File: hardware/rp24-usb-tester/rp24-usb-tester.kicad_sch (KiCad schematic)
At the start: 40 parts, among them J1 SPEAKER, J2 POWER, J3 EXT_CAP, J4 505070-2422, J5 RAILS, J6 AUX, J7 MOTOR, P1 USB_C_Receptacle_USB2.0_16P, Q1 SS8050, Q2 SS8050, Q3 SS8050, Q4 SS8050, Q5 SS8050, U1 MT2492

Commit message: chore: include 3d components
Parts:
- C1, C3: footprint Capacitor_SMD:C_0805_2012Metric -> rp24-usb-tester:C_0805_2012Metric
- C2: footprint Capacitor_SMD:C_0402_1005Metric -> rp24-usb-tester:C_0402_1005Metric
- D1, D10, D11, D12, D14, D2, D3, D4, D5, D6, D7, D8, D9: footprint LED_SMD:LED_0603_1608Metric -> rp24-usb-tester:LED_0603_1608Metric
- D13: footprint Diode_SMD:D_SMA -> rp24-usb-tester:D_SMA
- J1, J3, J5, J7: footprint Connector_PinHeader_2.54mm:PinHeader_1x02_P2.54mm_Vertical -> rp24-usb-tester:PinHeader_1x02_P2.54mm_Vertical
- J2: footprint Connector_PinHeader_2.54mm:PinHeader_1x04_P2.54mm_Vertical -> rp24-usb-tester:PinHeader_1x04_P2.54mm_Vertical
- J6: footprint Connector_PinHeader_2.54mm:PinHeader_1x05_P2.54mm_Vertical -> rp24-usb-tester:PinHeader_1x05_P2.54mm_Vertical
- P1: footprint Connector_USB:USB_C_Receptacle_GCT_USB4105-xx-A_16P_TopMnt_Horizontal -> rp24-usb-tester:USB_C_Receptacle_GCT_USB4105-xx-A_16P_TopMnt_Horizontal
- Q1, Q2, Q3, Q4, Q5: footprint Package_TO_SOT_SMD:SOT-23 -> rp24-usb-tester:SOT-23
- R1, R2, R5: footprint Resistor_SMD:R_0402_1005Metric -> rp24-usb-tester:R_0402_1005Metric
- R3, R4: footprint Resistor_SMD:R_0603_1608Metric -> rp24-usb-tester:R_0603_1608Metric
- RN1, RN2, RN3: footprint Resistor_SMD:R_Array_Concave_4x0402 -> rp24-usb-tester:R_Array_Concave_4x0402
- U1: footprint Package_TO_SOT_SMD:SOT-23-6 -> rp24-usb-tester:SOT-23-6
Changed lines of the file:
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@@
 			)
 		)
-		(property "Footprint" "Capacitor_SMD:C_0805_2012Metric"
+		(property "Footprint" "rp24-usb-tester:C_0805_2012Metric"
 			(at 109.5248 57.15 0)
 			(effects
@@
 			)
 		)
-		(property "Footprint" "Diode_SMD:D_SMA"
+		(property "Footprint" "rp24-usb-tester:D_SMA"
 			(at 189.23 57.785 0)
 			(effects
@@
 			)
 		)
-		(property "Footprint" "Resistor_SMD:R_0603_1608Metric"
+		(property "Footprint" "rp24-usb-tester:R_0603_1608Metric"
 			(at 159.258 59.69 90)
 			(effects
@@
 			)
 		)
-		(property "Footprint" "LED_SMD:LED_0603_1608Metric"
+		(property "Footprint" "rp24-usb-tester:LED_0603_1608Metric"
 			(at 38.1 148.59 0)
 			(effects
@@
 			)
 		)
-		(property "Footprint" "Resistor_SMD:R_0402_1005Metric"
+		(property "Footprint" "rp24-usb-tester:R_0402_1005Metric"
 			(at 87.63 51.308 90)
 			(effects
@@
 			)
 		)
-		(property "Footprint" "Connector_USB:USB_C_Receptacle_GCT_USB4105-xx-A_16P_TopMnt_Horizontal"
+		(property "Footprint" "rp24-usb-tester:USB_C_Receptacle_GCT_USB4105-xx-A_16P_TopMnt_Horizontal"
 			(at 63.5 57.15 0)
 			(effects
@@
 			)
 		)
-		(property "Footprint" "Package_TO_SOT_SMD:SOT-23"
+		(property "Footprint" "rp24-usb-tester:SOT-23"
 			(at 95.25 148.336 0)
 			(effects
@@
 			)
 		)
-		(property "Footprint" "LED_SMD:LED_0603_1608Metric"
+		(property "Footprint" "rp24-usb-tester:LED_0603_1608Metric"
 			(at 86.36 119.38 0)
 			(effects
@@
 			)
 		)
-		(property "Footprint" "Resistor_SMD:R_Array_Concave_4x0402"
+		(property "Footprint" "rp24-usb-tester:R_Array_Concave_4x0402"
 			(at 71.12 121.285 90)
 			(effects
@@
 			)
 		)
-		(property "Footprint" "Resistor_SMD:R_0402_1005Metric"
+		(property "Footprint" "rp24-usb-tester:R_0402_1005Metric"
 			(at 181.61 128.778 90)
 			(effects
@@
 			)
 		)
-		(property "Footprint" "LED_SMD:LED_0603_1608Metric"
+		(property "Footprint" "rp24-usb-tester:LED_0603_1608Metric"
 			(at 190.5 127 0)
 			(effects
@@
 			)
 		)
-		(property "Footprint" "LED_SMD:LED_0603_1608Metric"
+		(property "Footprint" "rp24-usb-tester:LED_0603_1608Metric"
 			(at 147.32 148.59 0)
 			(effects
@@
 			)
 		)
-		(property "Footprint" "Connector_PinHeader_2.54mm:PinHeader_1x02_P2.54mm_Vertical"
+		(property "Footprint" "rp24-usb-tester:PinHeader_1x02_P2.54mm_Vertical"
 			(at 232.41 148.59 0)
 			(effects
@@
 			)
 		)
-		(property "Footprint" "Capacitor_SMD:C_0805_2012Metric"
+		(property "Footprint" "rp24-usb-tester:C_0805_2012Metric"
 			(at 164.7952 57.15 0)
 			(effects
@@
 			)
 		)
-		(property "Footprint" "LED_SMD:LED_0603_1608Metric"
+		(property "Footprint" "rp24-usb-tester:LED_0603_1608Metric"
 			(at 38.1 160.02 0)
 			(effects
@@
 			)
 		)
-		(property "Footprint" "LED_SMD:LED_0603_1608Metric"
+		(property "Footprint" "rp24-usb-tester:LED_0603_1608Metric"
 			(at 38.1 125.73 0)
 			(effects
@@
 			)
 		)
-		(property "Footprint" "Connector_PinHeader_2.54mm:PinHeader_1x04_P2.54mm_Vertical"
+		(property "Footprint" "rp24-usb-tester:PinHeader_1x04_P2.54mm_Vertical"
 			(at 232.41 132.08 0)
 			(effects
@@
 			)
 		)
-		(property "Footprint" "LED_SMD:LED_0603_1608Metric"
+		(property "Footprint" "rp24-usb-tester:LED_0603_1608Metric"
 			(at 86.36 135.89 0)
 			(effects
@@
 			)
 		)
-		(property "Footprint" "Package_TO_SOT_SMD:SOT-23"
+		(property "Footprint" "rp24-usb-tester:SOT-23"
 			(at 201.93 141.986 0)
 			(effects
@@
 			)
 		)
-		(property "Footprint" "Resistor_SMD:R_Array_Concave_4x0402"
+		(property "Footprint" "rp24-usb-tester:R_Array_Concave_4x0402"
 			(at 128.27 137.795 90)
 			(effects
@@
 			)
 		)
-		(property "Footprint" "Package_TO_SOT_SMD:SOT-23"
+		(property "Footprint" "rp24-usb-tester:SOT-23"
 			(at 95.25 131.826 0)
 			(effects
@@
 			)
 		)
-		(property "Footprint" "LED_SMD:LED_0603_1608Metric"
+		(property "Footprint" "rp24-usb-tester:LED_0603_1608Metric"
 			(at 147.32 125.73 0)
 			(effects
@@
 			)
 		)
-		(property "Footprint" "Capacitor_SMD:C_0402_1005Metric"
+		(property "Footprint" "rp24-usb-tester:C_0402_1005Metric"
 			(at 142.24 44.7548 0)
 			(effects
@@
 			)
 		)
-		(property "Footprint" "Connector_PinHeader_2.54mm:PinHeader_1x02_P2.54mm_Vertical"
+		(property "Footprint" "rp24-usb-tester:PinHeader_1x02_P2.54mm_Vertical"
 			(at 232.41 116.84 0)
 			(effects
@@
 			)
 		)
-		(property "Footprint" "LED_SMD:LED_0603_1608Metric"
+		(property "Footprint" "rp24-usb-tester:LED_0603_1608Metric"
 			(at 86.36 152.4 0)
 			(effects
@@
 			)
 		)
-		(property "Footprint" "Package_TO_SOT_SMD:SOT-23-6"
+		(property "Footprint" "rp24-usb-tester:SOT-23-6"
 			(at 127 53.34 0)
 			(effects
@@
 			)
 		)
-		(property "Footprint" "LED_SMD:LED_0603_1608Metric"
+		(property "Footprint" "rp24-usb-tester:LED_0603_1608Metric"
 			(at 147.32 137.16 0)
 			(effects
@@
 			)
 		)
-		(property "Footprint" "Resistor_SMD:R_Array_Concave_4x0402"
+		(property "Footprint" "rp24-usb-tester:R_Array_Concave_4x0402"
 			(at 22.86 121.285 90)
 			(effects
@@
 			)
 		)
-		(property "Footprint" "LED_SMD:LED_0603_1608Metric"
+		(property "Footprint" "rp24-usb-tester:LED_0603_1608Metric"
 			(at 38.1 137.16 0)
 			(effects
@@
 			)
 		)
-		(property "Footprint" "Resistor_SMD:R_0402_1005Metric"
+		(property "Footprint" "rp24-usb-tester:R_0402_1005Metric"
 			(at 87.63 48.768 90)
 			(effects
@@
 			)
 		)
-		(property "Footprint" "LED_SMD:LED_0603_1608Metric"
+		(property "Footprint" "rp24-usb-tester:LED_0603_1608Metric"
 			(at 86.36 163.83 0)
 			(effects
@@
 			)
 		)
-		(property "Footprint" "LED_SMD:LED_0603_1608Metric"
+		(property "Footprint" "rp24-usb-tester:LED_0603_1608Metric"
 			(at 147.32 167.64 0)
 			(effects
@@
 			)
 		)
-		(property "Footprint" "Connector_PinHeader_2.54mm:PinHeader_1x02_P2.54mm_Vertical"
+		(property "Footprint" "rp24-usb-tester:PinHeader_1x02_P2.54mm_Vertical"
 			(at 257.81 116.84 0)
 			(effects
@@
 			)
 		)
-		(property "Footprint" "Connector_PinHeader_2.54mm:PinHeader_1x02_P2.54mm_Vertical"
+		(property "Footprint" "rp24-usb-tester:PinHeader_1x02_P2.54mm_Vertical"
 			(at 257.81 148.59 0)
 			(effects
@@
 			)
 		)
-		(property "Footprint" "Connector_PinHeader_2.54mm:PinHeader_1x05_P2.54mm_Vertical"
+		(property "Footprint" "rp24-usb-tester:PinHeader_1x05_P2.54mm_Vertical"
 			(at 257.81 134.62 0)
 			(effects
@@
 			)
 		)
-		(property "Footprint" "Resistor_SMD:R_0603_1608Metric"
+		(property "Footprint" "rp24-usb-tester:R_0603_1608Metric"
 			(at 159.258 52.07 90)
 			(effects
@@
 			)
 		)
-		(property "Footprint" "Package_TO_SOT_SMD:SOT-23"
+		(property "Footprint" "rp24-usb-tester:SOT-23"
 			(at 154.94 180.086 0)
 			(effects
@@
 			)
 		)
-		(property "Footprint" "Package_TO_SOT_SMD:SOT-23"
+		(property "Footprint" "rp24-usb-tester:SOT-23"
 			(at 154.94 161.036 0)
 			(effects

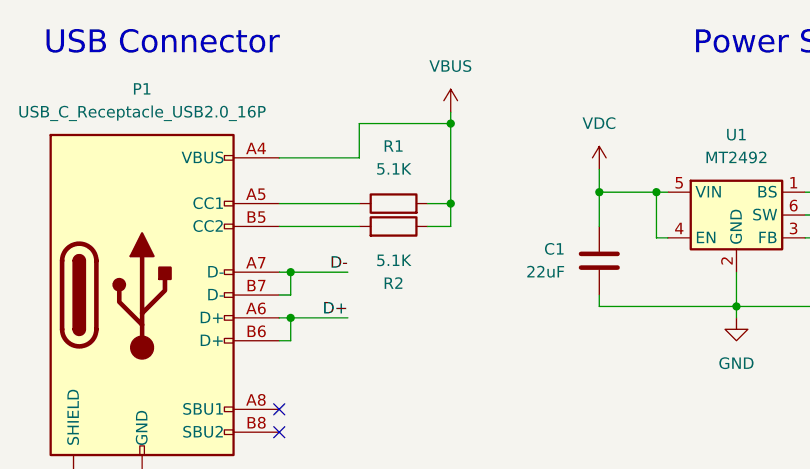
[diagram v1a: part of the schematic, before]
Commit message: fix: 5.1k resistors go to gnd
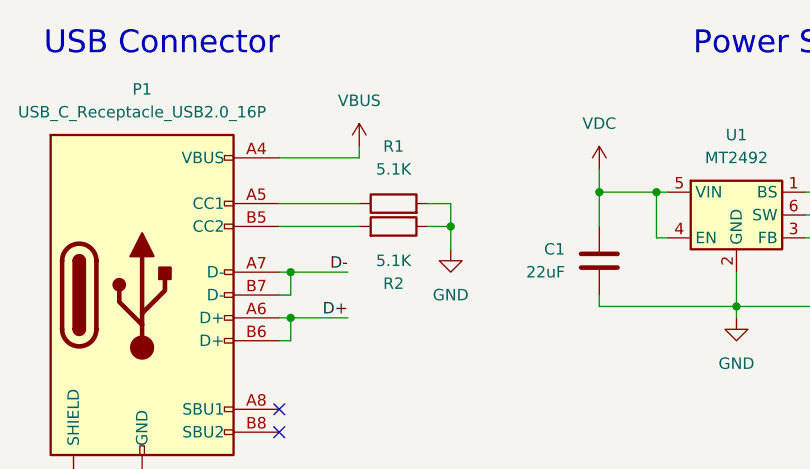
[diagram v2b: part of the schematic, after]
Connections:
- net GND: now also R1.2, R2.1
- net VBUS: no longer R1.2, R2.1
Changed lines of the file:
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@@
 	)
 	(junction
-		(at 93.98 46.99)
-		(diameter 0)
-		(color 0 0 0 0)
-	)
-	(junction
 		(at 157.48 48.26)
 		(diameter 0)
@@
 	)
 	(junction
-		(at 93.98 38.1)
-		(diameter 0)
-		(color 0 0 0 0)
-	)
-	(junction
 		(at 120.65 125.73)
 		(diameter 0)
@@
 	)
 	(junction
+		(at 93.98 49.53)
+		(diameter 0)
+		(color 0 0 0 0)
+	)
+	(junction
 		(at 163.83 48.26)
 		(diameter 0)
@@
 	(wire
 		(pts
-			(xy 83.82 38.1) (xy 93.98 38.1)
-		)
-		(stroke
-			(width 0)
-			(type default)
-		)
-	)
-	(wire
-		(pts
 			(xy 81.28 119.38) (xy 81.28 125.73)
 		)
@@
 	(wire
 		(pts
-			(xy 93.98 36.83) (xy 93.98 38.1)
-		)
-		(stroke
-			(width 0)
-			(type default)
-		)
-	)
-	(wire
-		(pts
 			(xy 120.65 128.27) (xy 120.65 125.73)
 		)
@@
 	(wire
 		(pts
+			(xy 83.82 40.64) (xy 83.82 41.91)
+		)
+		(stroke
+			(width 0)
+			(type default)
+		)
+	)
+	(wire
+		(pts
 			(xy 157.48 167.64) (xy 151.13 167.64)
 		)
@@
 	(wire
 		(pts
+			(xy 93.98 52.07) (xy 93.98 49.53)
+		)
+		(stroke
+			(width 0)
+			(type default)
+		)
+	)
+	(wire
+		(pts
 			(xy 248.92 44.45) (xy 264.16 44.45)
 		)
@@
 	(wire
 		(pts
-			(xy 93.98 38.1) (xy 93.98 46.99)
-		)
-		(stroke
-			(width 0)
-			(type default)
-		)
-	)
-	(wire
-		(pts
 			(xy 74.93 59.69) (xy 76.2 59.69)
 		)
@@
 	(wire
 		(pts
-			(xy 83.82 38.1) (xy 83.82 41.91)
-		)
-		(stroke
-			(width 0)
-			(type default)
-		)
-	)
-	(wire
-		(pts
 			(xy 137.16 167.64) (xy 143.51 167.64)
 		)
@@
 	)
 	(symbol
+		(lib_id "rp24-usb-tester:GND")
+		(at 93.98 52.07 0)
+		(unit 1)
+		(exclude_from_sim no)
+		(in_bom yes)
+		(on_board yes)
+		(dnp no)
+		(fields_autoplaced yes)
+		(property "Reference" "#PWR026"
+			(at 93.98 58.42 0)
+			(effects
+				(font
+					(size 1.27 1.27)
+				)
+				(hide yes)
+			)
+		)
+		(property "Value" "GND"
+			(at 93.98 57.15 0)
+			(effects
+				(font
+					(size 1.27 1.27)
+				)
+			)
+		)
+		(property "Footprint" ""
+			(at 93.98 52.07 0)
+			(effects
+				(font
+					(size 1.27 1.27)
+				)
+				(hide yes)
+			)
+		)
+		(property "Datasheet" ""
+			(at 93.98 52.07 0)
+			(effects
+				(font
+					(size 1.27 1.27)
+				)
+				(hide yes)
+			)
+		)
+		(property "Description" "Power symbol creates a global label with name \"GND\" , ground"
+			(at 93.98 52.07 0)
+			(effects
+				(font
+					(size 1.27 1.27)
+				)
+				(hide yes)
+			)
+		)
+		(pin "1"
+		)
+		(instances
+			(project "rp24-usb-tester"
+				(path "/d0286ab8-587a-4050-861e-41c0709ea38c"
+					(reference "#PWR026")
+					(unit 1)
+				)
+			)
+		)
+	)
+	(symbol
 		(lib_id "rp24-usb-tester:SS8050")
 		(at 196.85 134.62 0)
@@
 	(symbol
 		(lib_id "rp24-usb-tester:VBUS")
-		(at 93.98 36.83 0)
+		(at 83.82 40.64 0)
 		(unit 1)
 		(exclude_from_sim no)
@@
 		(on_board yes)
 		(dnp no)
-		(fields_autoplaced yes)
 		(property "Reference" "#PWR04"
-			(at 93.98 40.64 0)
+			(at 83.82 44.45 0)
 			(effects
 				(font
@@
 		)
 		(property "Value" "VBUS"
-			(at 93.98 31.75 0)
+			(at 83.82 35.56 0)
 			(effects
 				(font
@@
 		)
 		(property "Footprint" ""
-			(at 93.98 36.83 0)
+			(at 83.82 40.64 0)
 			(effects
 				(font
@@
 		)
 		(property "Datasheet" ""
-			(at 93.98 36.83 0)
+			(at 83.82 40.64 0)
 			(effects
 				(font
@@
 		)
 		(property "Description" "Power symbol creates a global label with name \"VBUS\""
-			(at 93.98 36.83 0)
+			(at 83.82 40.64 0)
 			(effects
 				(font
@@
 		)
 		(property "Sim.Device" ""
-			(at 93.98 36.83 0)
+			(at 83.82 40.64 0)
 			(effects
 				(font
@@
 		)
 		(property "Sim.Pins" ""
-			(at 93.98 36.83 0)
+			(at 83.82 40.64 0)
 			(effects
 				(font
